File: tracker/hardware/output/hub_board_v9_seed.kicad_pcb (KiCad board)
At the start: 4 copper layers, 103 x 103 mm, 39 parts, among them U1 ESP32-S3-WROOM-1U-N8R8, U2 LoRa2021F33-2G4, U3 LoRa2021_Castellated, U4 SX1280, U5 MAX-M10S, U6 MS5611-01BA, U7 TPS7A02

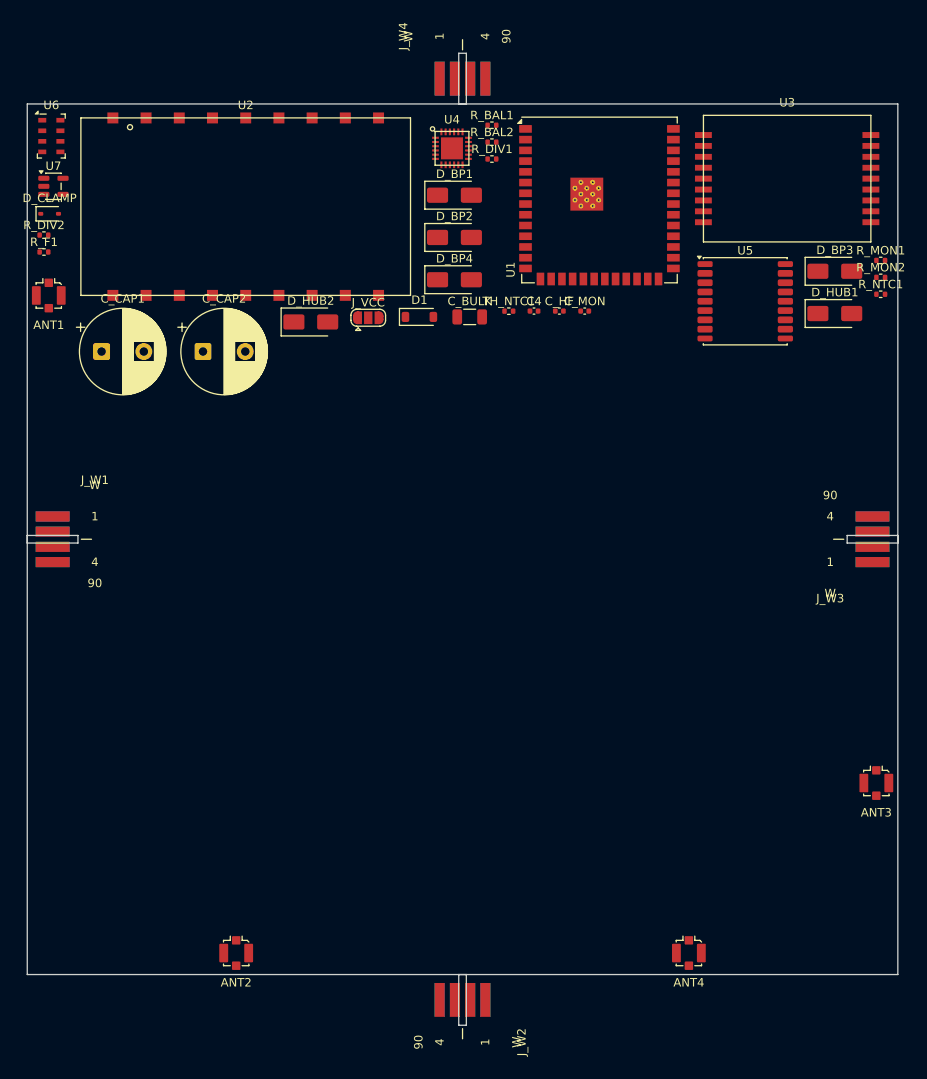
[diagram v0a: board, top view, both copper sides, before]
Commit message: feat(hw/hub): implement ADR-063 overhanging solar carrier
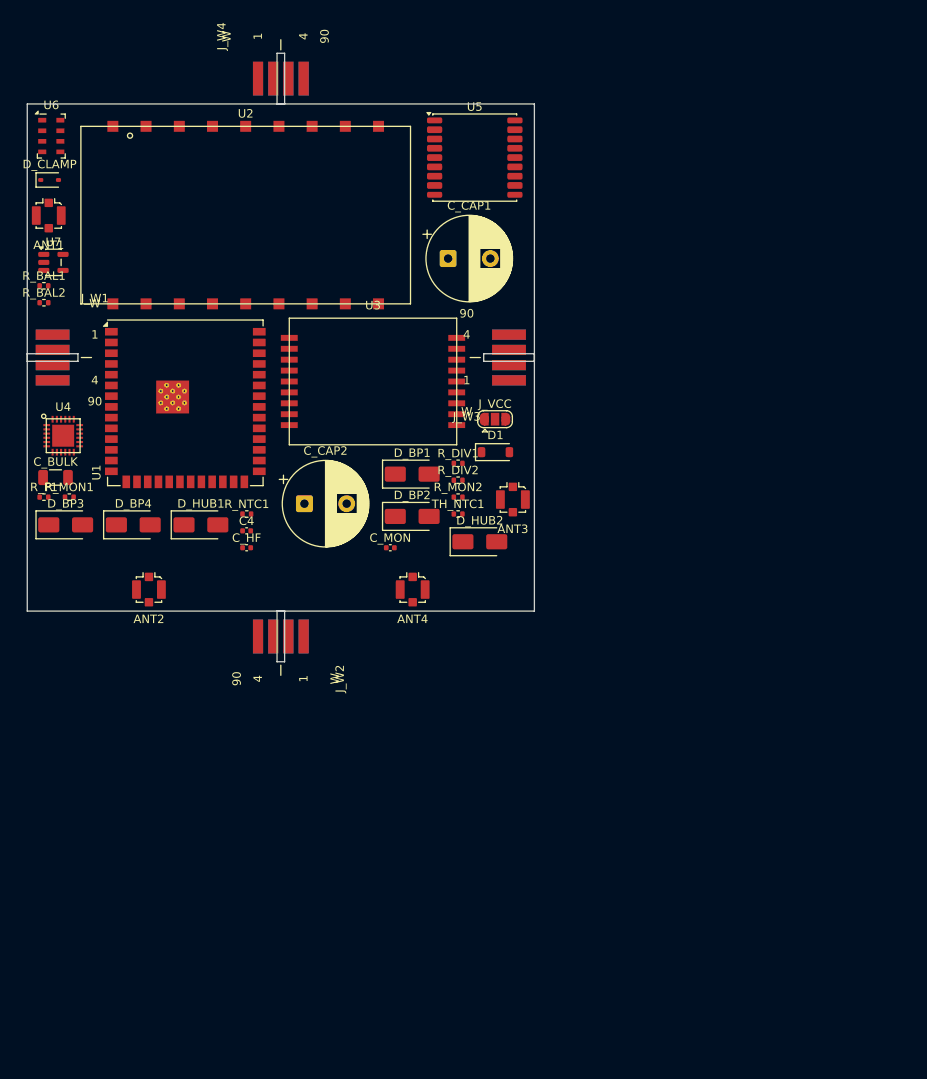
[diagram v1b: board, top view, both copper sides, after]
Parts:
- moved R_MON1 100.0 mm to (4.97, 46.5)
- moved D_BP3 95.8 mm to (4.54, 49.8)
- moved R_NTC1 79.4 mm to (26.0, 48.5)
- moved D_HUB1 79.1 mm to (20.5, 49.8)
- moved U4 57.2 mm to (4.25, 39.2)
- moved R_DIV2 56.9 mm to (51.0, 44.5)
- moved R_MON2 56.4 mm to (51.0, 46.5)
- moved R_BAL1 56.3 mm to (1.98, 21.5)
- moved R_BAL2 56.3 mm to (1.98, 23.5)
- moved U1 54.6 mm to (18.7, 35.4)
- moved U3 54.6 mm to (40.9, 32.8)
- moved ANT3 54.5 mm to (57.5, 46.8)
- moved ANT4 54.0 mm to (45.6, 57.5)
- moved C_BULK 52.6 mm to (3.35, 44.2)
- moved J_W2 48.1 mm to (30.0, 60.0)
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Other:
- board size 103 x 103 mm -> 60 x 60 mm
